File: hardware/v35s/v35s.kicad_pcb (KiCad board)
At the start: 2 copper layers, 99.1 x 99.1 mm, 13 parts, among them J1 nuMezzanine_4x34, U1 uPD70337L-8-xxx

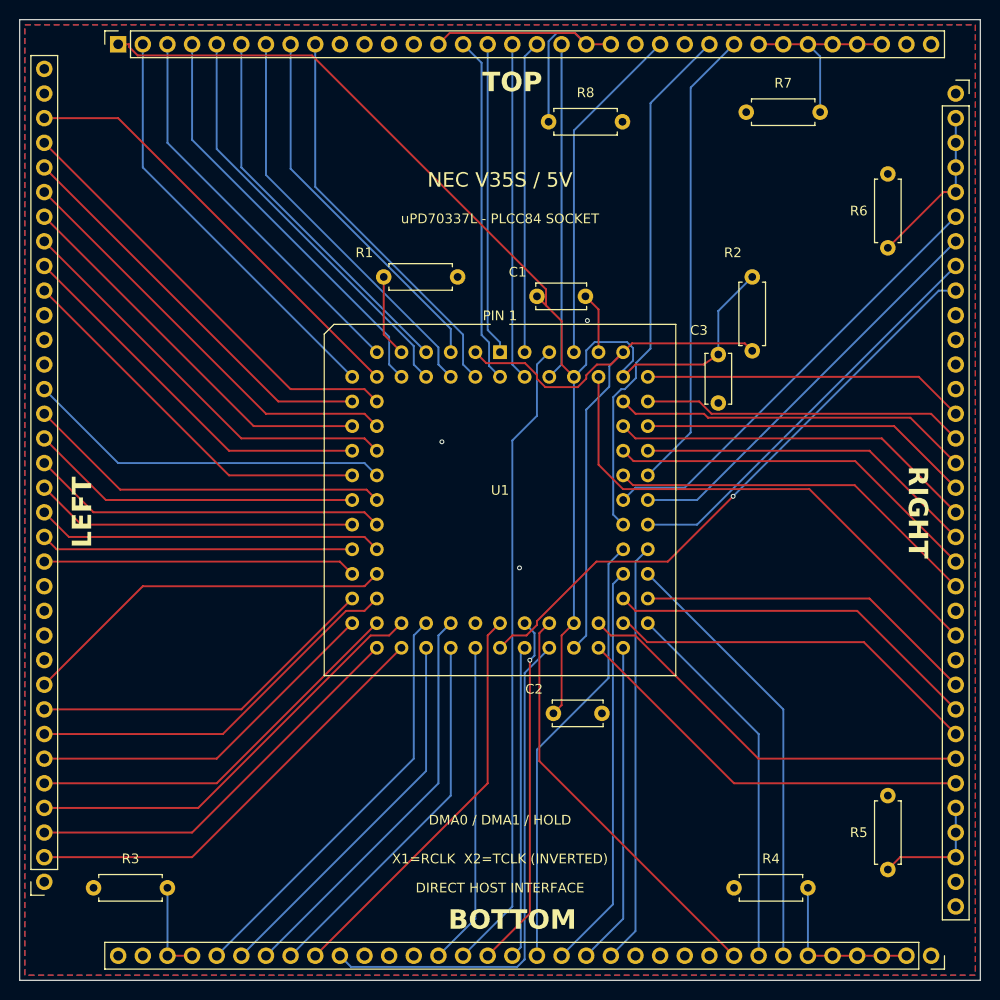
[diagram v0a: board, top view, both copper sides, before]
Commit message: Update mainboard to revision 2
Add an additional 8 bidirectional channels
Replace SPI PSRAM with hyperram
Remove LEDs
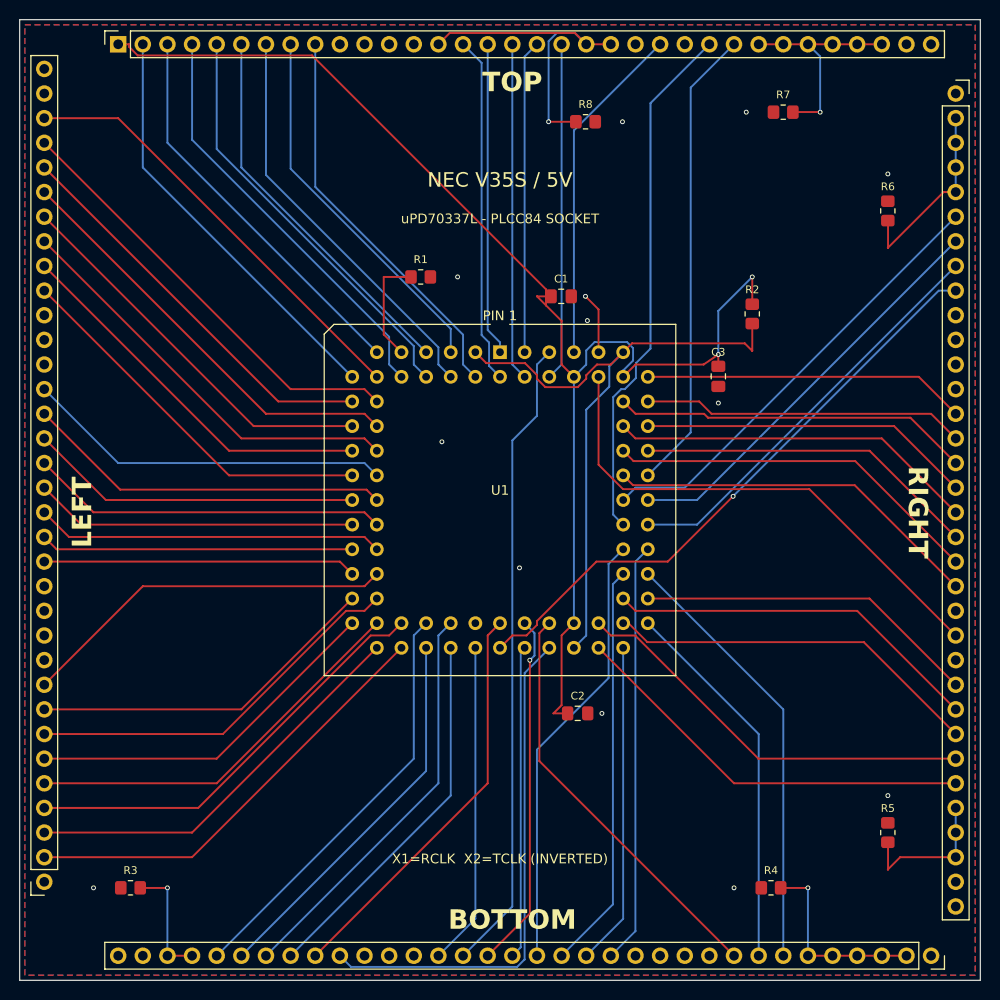
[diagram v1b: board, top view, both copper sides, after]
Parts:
- C1, C2, C3: footprint Capacitor_THT:C_Disc_D5.0mm_W2.5mm_P5.00mm -> Capacitor_SMD:C_0805_2012Metric_Pad1.18x1.45mm_HandSolder
- R1, R2, R3, R4, R5, R6, R7, R8: footprint Resistor_THT:R_Axial_DIN0207_L6.3mm_D2.5mm_P7.62mm_Horizontal -> Resistor_SMD:R_0805_2012Metric_Pad1.20x1.40mm_HandSolder
- moved R1 3.81 mm to (142.8, 73.0)
- moved R2 3.81 mm to (177.0, 76.8)
- moved R3 3.81 mm to (112.9, 136.0)
- moved R4 3.81 mm to (178.9, 136.0)
- moved R5 3.81 mm to (191.0, 130.3)
- moved R6 3.81 mm to (191.0, 66.2)
- moved R7 3.81 mm to (180.2, 56.0)
- moved R8 3.81 mm to (159.8, 57.0)
- moved C1 2.50 mm to (157.3, 75.0)
- moved C2 2.50 mm to (159.0, 118.0)
- moved C3 2.25 mm to (173.5, 83.2)
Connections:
- J1 pad 10: GND -> unconnected-(J1A-TX3-Pad10)
- J1 pad 102: unconnected-(J1E-NC-Pad102) -> GND
- J1 pad 112: GND -> unconnected-(J1B-LX3-Pad112)
- J1 pad 115: GND -> unconnected-(J1B-LX0-Pad115)
- J1 pad 13: GND -> unconnected-(J1A-TX0-Pad13)
- J1 pad 136: unconnected-(J1E-NC-Pad136) -> GND
- J1 pad 44: GND -> unconnected-(J1D-RX3-Pad44)
- J1 pad 47: GND -> unconnected-(J1D-RX0-Pad47)
- J1 pad 78: GND -> unconnected-(J1C-BX3-Pad78)
- J1 pad 81: GND -> unconnected-(J1C-BX0-Pad81)
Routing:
- net /VCC_TL: track 134.0 -> 141.0 mm, vias 0 -> 2
- net /R2_UNUSED: track 17.0 -> 19.8 mm
- net /R0_UNUSED: track 12.6 -> 15.4 mm
- net /B2_UNUSED: track 17.2 -> 20.0 mm, vias 0 -> 1
- net /IC_BIAS: track 65.2 -> 68.1 mm
- net /T0_UNUSED: track 20.2 -> 23.0 mm, vias 0 -> 1
- net /B0_UNUSED: track 9.54 -> 12.4 mm, vias 0 -> 1
- net /T1_UNUSED: track 31.8 -> 34.6 mm, vias 0 -> 1
- net /RESERVED_PD: track 8.52 -> 11.3 mm
- net GND: vias 3 -> 13
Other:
- board text removed: "DIRECT HOST INTERFACE"
- board text removed: "DMA0 / DMA1 / HOLD"
